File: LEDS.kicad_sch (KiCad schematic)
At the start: 22 parts, among them U801 74HC595, U802 74HC595

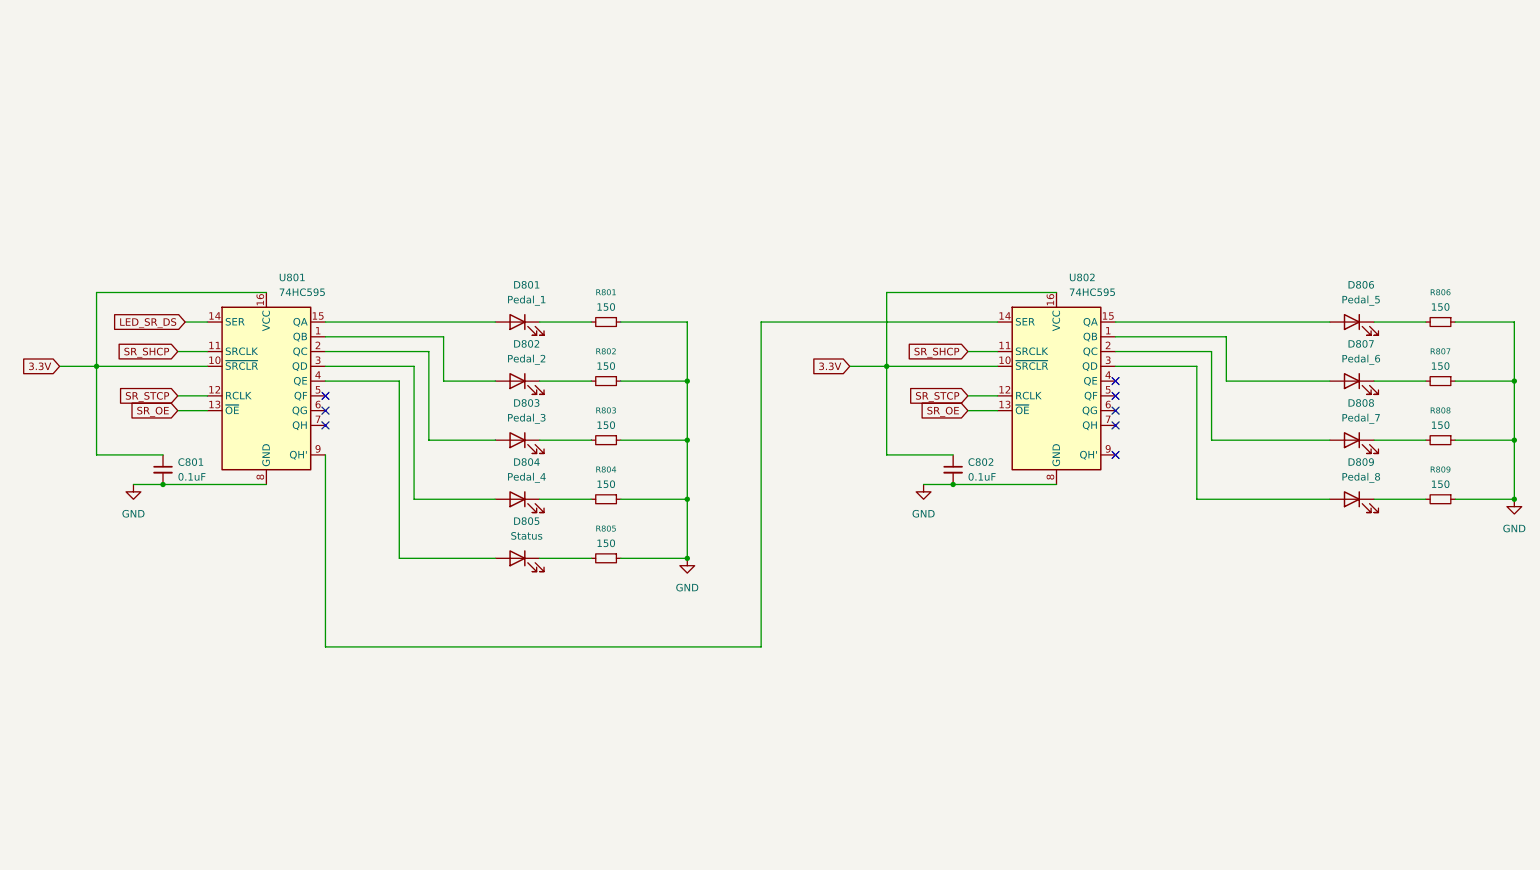
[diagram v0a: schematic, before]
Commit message: Removed LED Shift registers and replaced them with PCA9685 PWM controllers, Also changed LEDs to RGB LEDs.
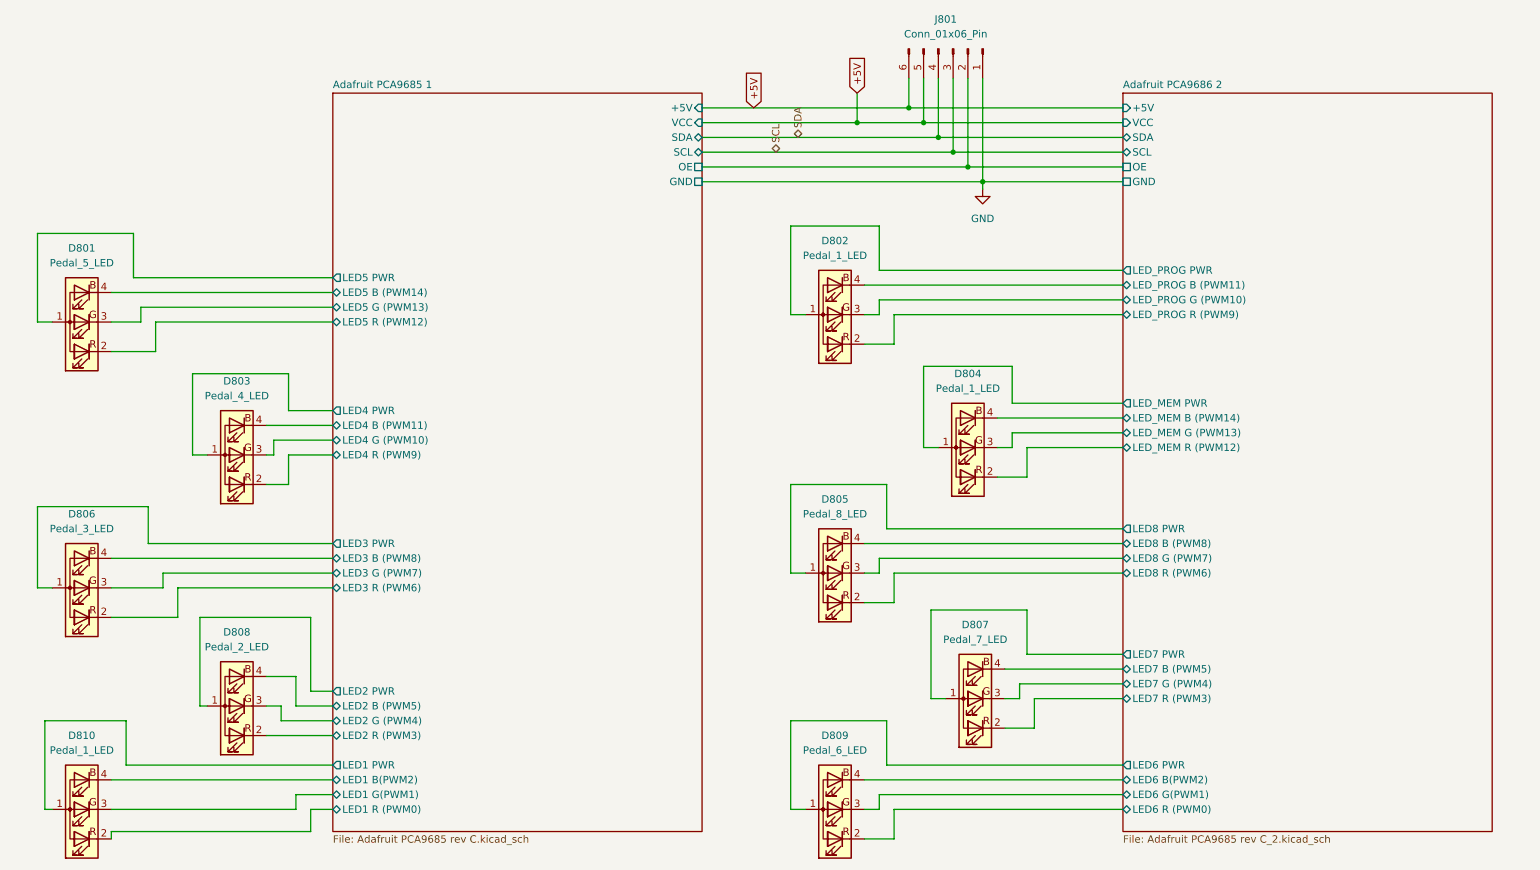
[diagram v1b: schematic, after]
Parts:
- removed C801, C802: 0.1uF, Capacitor_THT:C_Disc_D5.0mm_W2.5mm_P2.50mm, symbol Device:C_Small
- removed D801: Pedal_1, Connector_PinHeader_2.54mm:PinHeader_1x02_P2.54mm_Vertical, symbol Device:LED
- removed D802: Pedal_2, Connector_PinHeader_2.54mm:PinHeader_1x02_P2.54mm_Vertical, symbol Device:LED
- removed D803: Pedal_3, Connector_PinHeader_2.54mm:PinHeader_1x02_P2.54mm_Vertical, symbol Device:LED
- removed D804: Pedal_4, Connector_PinHeader_2.54mm:PinHeader_1x02_P2.54mm_Vertical, symbol Device:LED
- removed D805: Status, Connector_PinHeader_2.54mm:PinHeader_1x02_P2.54mm_Vertical, symbol Device:LED
- removed D806: Pedal_5, Connector_PinHeader_2.54mm:PinHeader_1x02_P2.54mm_Vertical, symbol Device:LED
- removed D807: Pedal_6, Connector_PinHeader_2.54mm:PinHeader_1x02_P2.54mm_Vertical, symbol Device:LED
- removed D808: Pedal_7, Connector_PinHeader_2.54mm:PinHeader_1x02_P2.54mm_Vertical, symbol Device:LED
- removed D809: Pedal_8, Connector_PinHeader_2.54mm:PinHeader_1x02_P2.54mm_Vertical, symbol Device:LED
- removed R801, R802, R803, R804, R805, R806, R807, R808, R809: 150, Resistor_THT:R_Axial_DIN0207_L6.3mm_D2.5mm_P7.62mm_Horizontal, symbol Device:R_Small
- removed U801, U802: 74HC595, Package_DIP:DIP-16_W7.62mm, symbol 74xx:74HC595
- added D801: Pedal_5_LED, symbol Device:LED_ARGB
- added D802, D804, D810: Pedal_1_LED, symbol Device:LED_ARGB
- added D803: Pedal_4_LED, symbol Device:LED_ARGB
- added D805: Pedal_8_LED, symbol Device:LED_ARGB
- added D806: Pedal_3_LED, symbol Device:LED_ARGB
- added D807: Pedal_7_LED, symbol Device:LED_ARGB
- added D808: Pedal_2_LED, symbol Device:LED_ARGB
- added D809: Pedal_6_LED, symbol Device:LED_ARGB
- added J801: Conn_01x06_Pin, Connector_PinHeader_2.54mm:PinHeader_1x06_P2.54mm_Vertical, symbol Connector:Conn_01x06_Pin
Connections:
- net GND: now also J801.1 (Pin_1)
- new net +5V: J801.5 (Pin_5), J801.6 (Pin_6)
- new net Adafruit PCA9685 1/LED1 B(PWM2): D810.4 (BK)
- new net Adafruit PCA9685 1/LED1 G(PWM1): D810.3 (GK)
- new net Adafruit PCA9685 1/LED1 PWR: D810.1 (A)
- new net Adafruit PCA9685 1/LED1 R (PWM0): D810.2 (RK)
- new net Adafruit PCA9685 1/LED2 B (PWM5): D808.4 (BK)
- new net Adafruit PCA9685 1/LED2 G (PWM4): D808.3 (GK)
- new net Adafruit PCA9685 1/LED2 PWR: D808.1 (A)
- new net Adafruit PCA9685 1/LED2 R (PWM3): D808.2 (RK)
- new net Adafruit PCA9685 1/LED3 B (PWM8): D806.4 (BK)
- new net Adafruit PCA9685 1/LED3 G (PWM7): D806.3 (GK)
- new net Adafruit PCA9685 1/LED3 PWR: D806.1 (A)
- new net Adafruit PCA9685 1/LED3 R (PWM6): D806.2 (RK)
- new net Adafruit PCA9685 1/LED4 B (PWM11): D803.4 (BK)
- new net Adafruit PCA9685 1/LED4 G (PWM10): D803.3 (GK)
- new net Adafruit PCA9685 1/LED4 PWR: D803.1 (A)
- new net Adafruit PCA9685 1/LED4 R (PWM9): D803.2 (RK)
- new net Adafruit PCA9685 1/LED5 B (PWM14): D801.4 (BK)
- new net Adafruit PCA9685 1/LED5 G (PWM13): D801.3 (GK)
- new net Adafruit PCA9685 1/LED5 PWR: D801.1 (A)
- new net Adafruit PCA9685 1/LED5 R (PWM12): D801.2 (RK)
- new net Adafruit PCA9685 1/OE: J801.2 (Pin_2)
- new net Adafruit PCA9686 2/LED6 B(PWM2): D809.4 (BK)
- new net Adafruit PCA9686 2/LED6 G(PWM1): D809.3 (GK)
- new net Adafruit PCA9686 2/LED6 PWR: D809.1 (A)
- new net Adafruit PCA9686 2/LED6 R (PWM0): D809.2 (RK)
- new net Adafruit PCA9686 2/LED7 B (PWM5): D807.4 (BK)
- new net Adafruit PCA9686 2/LED7 G (PWM4): D807.3 (GK)
- new net Adafruit PCA9686 2/LED7 PWR: D807.1 (A)
- new net Adafruit PCA9686 2/LED7 R (PWM3): D807.2 (RK)
- new net Adafruit PCA9686 2/LED8 B (PWM8): D805.4 (BK)
- new net Adafruit PCA9686 2/LED8 G (PWM7): D805.3 (GK)
- new net Adafruit PCA9686 2/LED8 PWR: D805.1 (A)
- new net Adafruit PCA9686 2/LED8 R (PWM6): D805.2 (RK)
- new net Adafruit PCA9686 2/LED_MEM B (PWM14): D804.4 (BK)
- new net Adafruit PCA9686 2/LED_MEM G (PWM13): D804.3 (GK)
- new net Adafruit PCA9686 2/LED_MEM PWR: D804.1 (A)
- new net Adafruit PCA9686 2/LED_MEM R (PWM12): D804.2 (RK)
- new net Adafruit PCA9686 2/LED_PROG B (PWM11): D802.4 (BK)
- new net Adafruit PCA9686 2/LED_PROG G (PWM10): D802.3 (GK)
- new net Adafruit PCA9686 2/LED_PROG PWR: D802.1 (A)
- new net Adafruit PCA9686 2/LED_PROG R (PWM9): D802.2 (RK)
- new net SCL: J801.3 (Pin_3)
- new net SDA: J801.4 (Pin_4)
- no-connect marks 8 -> 0
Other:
- added sheet Adafruit PCA9685 1 (Adafruit PCA9685 rev C.kicad_sch)
- added sheet Adafruit PCA9686 2 (Adafruit PCA9685 rev C_2.kicad_sch)
